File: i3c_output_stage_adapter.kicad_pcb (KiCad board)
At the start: 2 copper layers, 61 x 49.5 mm, 52 parts, among them J1 PinSocket_2x12_P2.54mm_Drill1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, J2 PinSocket_2x6_P2.54mm_Drill1.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, J3 Molex_Nano-Fit_1x2_SMD_105430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, J4 PinHeader_2x5_P1.27mm_SMD, J5 PinHeader_2x5_P1.27mm_SMD, J6 JST_XH_1x3_S3B-XH-A-LF-SN, Q1 DMC2400UV-7, Q2 DMC2400UV-7, Q3 DMC2400UV-7, Q4 DMC2400UV-7, U1 TPS7A0518P_SOT23-5, U2 SN74LVC1G240_SC70, U3 SN74LVC1G240_SC70

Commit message: [#68164] Clean DRC
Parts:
- removed D3: LED_G_0402_VLMTG1500-GS08, antmicro-footprints:LED_0402_1005Metric_G
- removed J4, J5: PinHeader_2x5_P1.27mm_SMD, antmicro-footprints:PinHeader_2x5_P1.27mm_SMD
- added J7: PinHeader_2x10_P1.27mm_SMD, antmicro-footprints:PinHeader_2x10_P1.27mm_SMD, B.Cu at (162.8, 112.0)
- added MP1: MP_Pad6mm_Drill3.2mm, antmicro-footprints:MP_Pad6mm_Drill3.2mm, F.Cu at (168.5, 76.0)
- added MP2: MP_Pad6mm_Drill3.2mm, antmicro-footprints:MP_Pad6mm_Drill3.2mm, F.Cu at (168.5, 105.0)
- added MP3: MP_Pad6mm_Drill3.2mm, antmicro-footprints:MP_Pad6mm_Drill3.2mm, F.Cu at (124.0, 86.5)
- added MP4: MP_Pad6mm_Drill3.2mm, antmicro-footprints:MP_Pad6mm_Drill3.2mm, F.Cu at (124.0, 118.5)
- added R20: R_10k_0402, antmicro-footprints:R_0402_1005Metric, F.Cu at (134.7, 99.6)
- added R21: R_0R_0402, antmicro-footprints:R_0402_1005Metric, F.Cu at (134.7, 97.6)
- added R22: R_2k_0402, antmicro-footprints:R_0402_1005Metric, F.Cu at (132.8, 111.8)
- added R23: R_2k_0402, antmicro-footprints:R_0402_1005Metric, F.Cu at (132.9, 108.4)
- added R24: R_10k_0402, antmicro-footprints:R_0402_1005Metric, F.Cu at (134.7, 111.6)
- added R25: R_0R_0402, antmicro-footprints:R_0402_1005Metric, F.Cu at (134.7, 109.6)
- Q1, Q2: value DMC2400UV-7 -> DMC31D5UDJ; footprint antmicro-footprints:SOT-563 -> antmicro-footprints:SOT-963
- R10, R19: value R_2k_0402 -> R_10k_0402
- R9: value R_2k_0402 -> R_0R_0402
- moved R19 32.1 mm to (131.1, 98.8), turned to 90 degrees
- moved R15 13.6 mm to (131.1, 96.8)
- moved TP3 6.34 mm to (163.8, 119.4)
- moved C1 5.51 mm to (141.0, 78.2), turned to -90 degrees
- moved J6 4.72 mm to (164.7, 98.0), turned to 90 degrees
- moved J1 4.66 mm to (110.0, 120.2)
- moved R16 4.05 mm to (136.0, 80.5)
- moved R10 3.84 mm to (131.1, 110.8), turned to 90 degrees
- moved R9 3.80 mm to (131.1, 108.8)
- moved J3 3.76 mm to (130.0, 76.5)
- moved R4 3.66 mm to (123.4, 110.5), turned to -90 degrees
- moved R8 3.48 mm to (125.8, 112.0), turned to 0 degrees
- moved R6 3.44 mm to (126.0, 109.1), turned to 90 degrees
- moved TP1 3.19 mm to (170.2, 119.4)
- moved TP2 3.19 mm to (167.0, 119.4)
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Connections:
- C3 pad 2: VCC -> +1V8
- C4 pad 2: VCC -> +1V8
- F1 pad 2: VCC -> +1V8
- F2 pad 2: VCC -> +1V8
- J3 pad 1: VCC -> +1V8
- J6 pad 1: /SDA -> /SCL
- J6 pad 3: /SCL -> /SDA
- Q3 pad 2: /SCL_DOWN -> Net-(Q3-G1)
- Q3 pad 4: Net-(Q3-D1) -> /SCL
- Q3 pad 5: /SCL_UP -> Net-(Q3-G2)
- Q3 pad 6: Net-(Q3-D1) -> /SCL
- Q4 pad 2: /SDA_DOWN -> Net-(Q4-G1)
- Q4 pad 5: /SDA_UP -> Net-(Q4-G2)
- R10 pad 2: Net-(Q3-S1) -> Net-(Q3-G1)
- R11 pad 2: VCC -> +1V8
- R13 pad 2: VCC -> +1V8
- R14 pad 2: VCC -> +1V8
- R15 pad 1: +3V3 -> /SDA_DOWN
- R15 pad 2: VCC -> Net-(Q4-G1)
- R16 pad 2: VCC -> +1V8
- R17 pad 2: /1V8_LDO -> +1V8
- R19 pad 1: Net-(D3-A) -> GND
- R19 pad 2: VCC -> Net-(Q4-G1)
- R5 pad 2: VCC -> +1V8
- R6 pad 2: VCC -> +1V8
- R9 pad 1: Net-(Q3-D2) -> /SCL_DOWN
- R9 pad 2: VCC -> Net-(Q3-G1)
- U2 pad 5: VCC -> +1V8
- U3 pad 5: VCC -> +1V8
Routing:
- net /SCL: track 0.00 -> 121.7 mm, vias 0 -> 5
- net /SDA: track 0.00 -> 110.2 mm, vias 0 -> 4
- net /SDA_EN/PULL: track 0.00 -> 94.4 mm, vias 0 -> 3
- net /SDA_IN/PUSH: track 0.00 -> 88.3 mm, vias 0 -> 4
- net /SDA_DOWN: track 0.00 -> 84.4 mm, vias 0 -> 3
- net /SCL_DOWN: track 0.00 -> 83.9 mm, vias 0 -> 2
- net /SDA_UP: track 0.00 -> 81.1 mm, vias 0 -> 3
- net /SCL_EN/PULL: track 0.00 -> 80.2 mm, vias 0 -> 2
- net /SCL_UP: track 0.00 -> 79.2 mm, vias 0 -> 2
- net /SCL_IN/PUSH: track 0.00 -> 77.4 mm, vias 0 -> 2
- net GND: track 0.00 -> 43.4 mm, vias 0 -> 31
- net +3V3: track 0.00 -> 32.6 mm
- net +1V8: track 0.00 -> 22.2 mm, vias 0 -> 17
- net /1V8_LDO: track 0.00 -> 4.21 mm
- net Net-(Q2-G2): track 0.00 -> 3.98 mm
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- added copper zone on In1.Cu, net +1V8
- added copper zone on In2.Cu, net GND
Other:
- board size 61 x 49.5 mm -> 72.5 x 50 mm
- copper layers 2 -> 4
- board text added: "1V8 IN"
- board text added: "I3C OUTPUT"
- board text added: "LOGIC ANALYZER CONNECTOR"
- board text added: "PMOD"
- board text removed: "VCC"

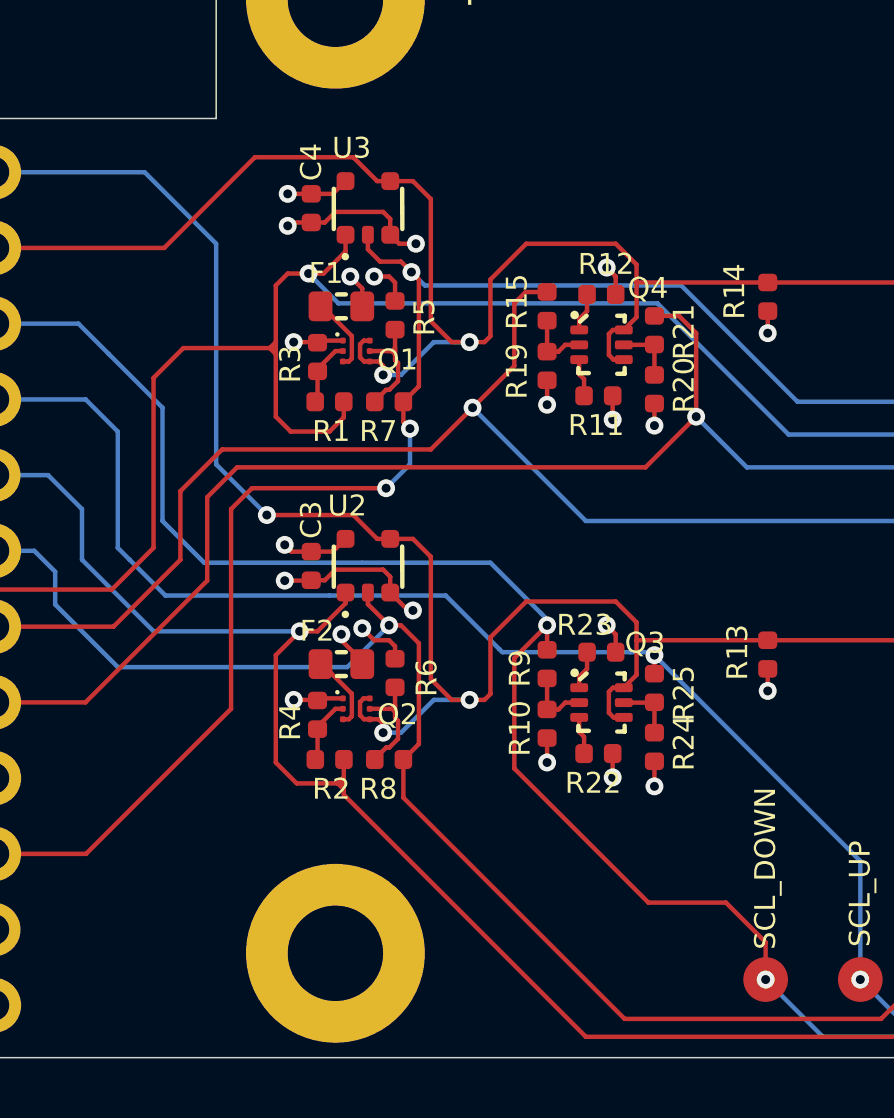
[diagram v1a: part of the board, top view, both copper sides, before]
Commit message: [#68164] Update PMOS connections on PCB
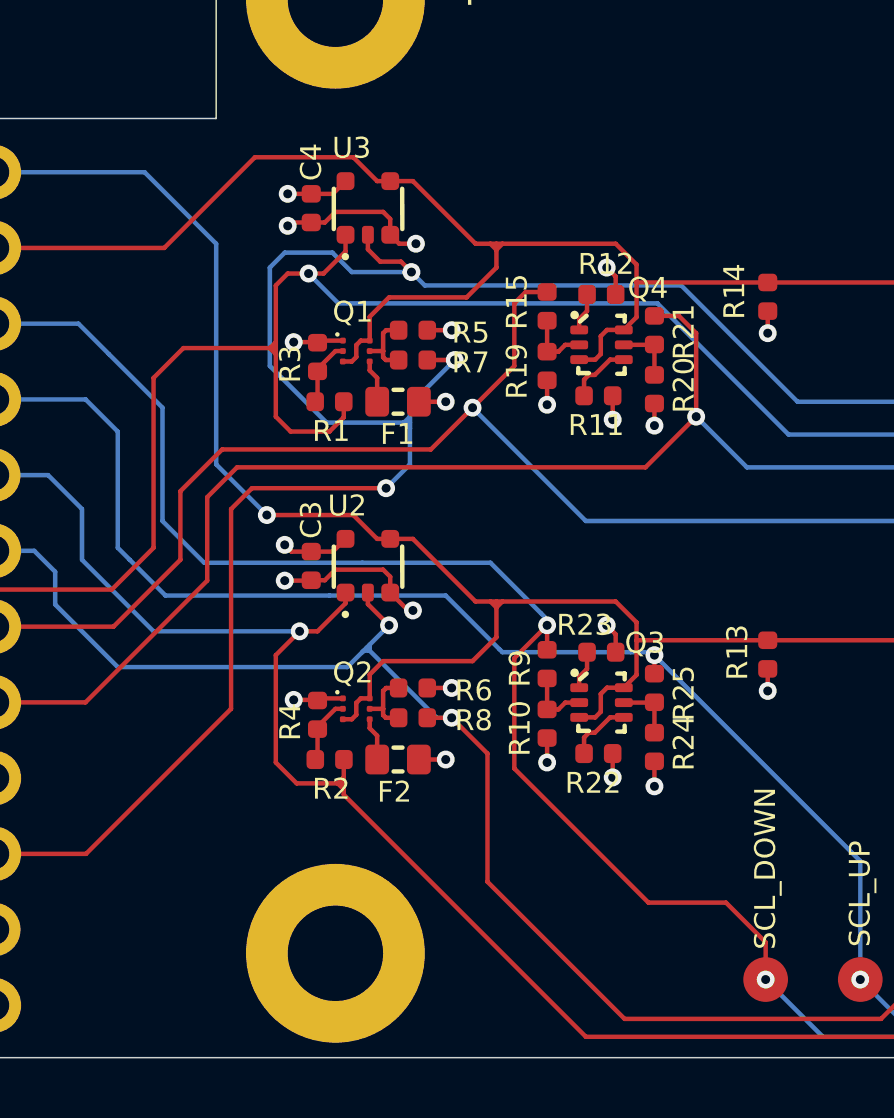
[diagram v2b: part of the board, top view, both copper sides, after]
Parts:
- moved F1 3.72 mm to (126.1, 100.0)
- moved F2 3.72 mm to (126.1, 112.0)
- moved R7 1.61 mm to (126.6, 98.6)
- moved R8 1.61 mm to (126.6, 110.6)
- moved R5 0.78 mm to (126.6, 97.6), turned to 0 degrees
- moved R6 0.78 mm to (126.6, 109.6), turned to 0 degrees
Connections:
- F1 pad 1: Net-(Q1-D2) -> Net-(Q1-S2)
- F2 pad 1: Net-(Q2-D2) -> Net-(Q2-S2)
- Q1 pad 3: Net-(Q1-D2) -> /SDA
- Q1 pad 4: /SDA -> Net-(Q1-S2)
- Q2 pad 3: Net-(Q2-D2) -> /SCL
- Q2 pad 4: /SCL -> Net-(Q2-S2)
- Q3 pad 3: Net-(Q3-D2) -> /SCL
- Q3 pad 4: /SCL -> Net-(Q3-S2)
- Q4 pad 3: Net-(Q4-D2) -> /SDA
- Q4 pad 4: /SDA -> Net-(Q4-S2)
- R11 pad 1: Net-(Q4-D2) -> Net-(Q4-S2)
- R22 pad 1: Net-(Q3-D2) -> Net-(Q3-S2)
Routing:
- net /SDA_IN/PUSH: track 88.3 -> 101.1 mm
- net /SDA: track 110.2 -> 107.5 mm, vias 4 -> 2
- net Net-(Q2-D2): track 2.56 -> 0.00 mm
- net Net-(Q1-D2): track 2.56 -> 0.00 mm
- net /SCL: track 121.7 -> 119.3 mm, vias 5 -> 3
- net +1V8: track 22.2 -> 20.0 mm
- net Net-(Q4-S2): track 0.00 -> 2.15 mm
- net Net-(Q3-S2): track 0.00 -> 2.15 mm
- net Net-(Q2-G2): track 3.98 -> 2.38 mm
- net Net-(Q1-G2): track 3.98 -> 2.38 mm
- net Net-(Q2-S2): track 0.00 -> 1.45 mm
- net Net-(Q1-S2): track 0.00 -> 1.45 mm
- net Net-(Q4-D2): track 1.28 -> 0.00 mm
- net Net-(Q3-D2): track 1.28 -> 0.00 mm
- net /SCL_IN/PUSH: track 77.4 -> 77.9 mm, vias 2 -> 3

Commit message: [#68164] Add logos, align mounting holes
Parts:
- added REF**: LOGO, antmicro-footprints:oshw-logo, F.Cu at (156.4, 105.1)
- added REF**: LOGO, antmicro-footprints:antmicro-logo_scaled_12mm, F.Cu at (138.6, 89.8)
- moved MP2 13.5 mm to (168.5, 118.5)
- moved MP3 10.5 mm to (124.0, 76.0)
- moved TP1 7.77 mm to (162.4, 119.4)
- moved TP11 7.77 mm to (130.7, 119.4)
- moved TP3 7.77 mm to (156.1, 119.4)
- moved TP4 7.77 mm to (152.9, 119.4)
- moved TP5 7.77 mm to (149.7, 119.4)
- moved TP7 7.77 mm to (143.3, 119.4)
- moved TP8 7.77 mm to (140.2, 119.4)
- moved TP9 7.77 mm to (137.0, 119.4)
- moved TP10 7.77 mm to (133.8, 119.4)
- moved TP2 7.77 mm to (159.2, 119.4)
- moved TP6 7.77 mm to (146.5, 119.4)
- moved J7 2.84 mm to (162.8, 109.1)
- moved C1 2.49 mm to (143.5, 78.2)
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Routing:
- net /SDA: track 107.5 -> 101.4 mm
- net /SCL: track 119.3 -> 124.6 mm
- net /SCL_UP: track 79.2 -> 83.9 mm
- net /SDA_EN/PULL: track 94.4 -> 97.5 mm
- net +3V3: track 32.6 -> 30.1 mm
- net /SCL_DOWN: track 83.9 -> 85.9 mm
- net /SDA_UP: track 81.1 -> 82.2 mm
- net /SDA_IN/PUSH: track 101.1 -> 100.2 mm
- net /SCL_EN/PULL: track 80.2 -> 81.0 mm
- net /SDA_DOWN: track 84.4 -> 85.0 mm
- net /SCL_IN/PUSH: track 77.9 -> 78.5 mm
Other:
- board text added: "I3C Output Stage Adapter"
- board text added: "Rev. ${REVISION}"
- board text added: "SHA: ########"

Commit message: [#68164] Apply changes to PCB
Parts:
- added C5: C_10n_0402, antmicro-footprints:C_0402_1005Metric, F.Cu at (148.3, 99.6)
- added C6: C_100n_16V_X7R_0402, antmicro-footprints:C_0402_1005Metric, F.Cu at (150.1, 101.8)
- added C7: C_1u_0603, antmicro-footprints:C_0603_1608Metric, F.Cu at (135.1, 125.5)
- added C8: C_1u_0603, antmicro-footprints:C_0603_1608Metric, F.Cu at (135.0, 121.2)
- added C9: C_1u_0603, antmicro-footprints:C_0603_1608Metric, F.Cu at (135.0, 119.8)
- added D3: LED_G_0402_VLMTG1500-GS08, antmicro-footprints:LED_0402_1005Metric_G, F.Cu at (141.7, 96.4)
- added J4: USB-C_CUI_UJC-HP-3-SMT-TR, antmicro-footprints:USB-C_Receptacle_CUI_UJC-HP-3-SMT-TR, F.Cu at (148.0, 94.5)
- added J5: PinHeader_1x3_P2.54mm_Drill1.1mm, antmicro-footprints:PinHeader_1x3_P2.54mm_Drill1.1mm, F.Cu at (131.5, 120.5)
- added L1: FB_120Z_2A_Murata-BLM18PG_0603, antmicro-footprints:FB_0603_1608Metric, F.Cu at (151.7, 99.3)
- added L2: FB_120Z_2A_Murata-BLM18PG_0603, antmicro-footprints:FB_0603_1608Metric, F.Cu at (149.6, 99.9)
- added Q5: DMG1012T-7, antmicro-footprints:SOT-523, F.Cu at (135.2, 96.6)
- added R26: R_5k1_0402, antmicro-footprints:R_0402_1005Metric, F.Cu at (147.2, 99.6)
- added R27: R_5k1_0402, antmicro-footprints:R_0402_1005Metric, F.Cu at (146.0, 99.6)
- added R28: 4x0R_0402_array, antmicro-footprints:4x0R_0402_array_EXB28V, F.Cu at (105.2, 109.0)
- added R29: R_2k_0402, antmicro-footprints:R_0402_1005Metric, F.Cu at (141.7, 98.6)
- added R30: R_10k_0402, antmicro-footprints:R_0402_1005Metric, F.Cu at (135.2, 98.5)
- added REF**: Jumper_1x2_P2.54mm, antmicro-footprints:Jumper_1x2_P2.54mm, F.Cu at (129.0, 120.5)
- added U4: TLV70033_SC70, antmicro-footprints:SC-70-5, F.Cu at (135.1, 123.4)
- J1, J2: moved to B.Cu
- J3: value Molex_Nano-Fit_1x2_SMD_1054301202 -> JST_SH_1x4_SM04B-SRSS-TB-LF-SN; footprint antmicro-footprints:Conn_Molex_Nano-Fit_1x2_SMD_1054301202 -> antmicro-footprints:Conn_JST_SH_1x4_SM04B-SRSS-TB-LF-SN
- J6: value JST_XH_1x3_S3B-XH-A-LF-SN -> PinHeader_1x3_P2.54mm_Drill1.1mm_Horizontal; footprint antmicro-footprints:Conn_JST_XH_1x3_S3B-XH-A-LF-SN -> antmicro-footprints:PinHeader_1x3_P2.54mm_Horizontal
- J7: moved to F.Cu
- moved C1 48.7 mm to (127.7, 124.2), turned to 90 degrees
- moved J3 48.4 mm to (172.0, 104.5), turned to 90 degrees
- moved J2 47.4 mm to (110.0, 112.6), turned to -90 degrees
- moved U1 47.3 mm to (130.1, 124.2), turned to -90 degrees
- moved C2 47.2 mm to (132.6, 125.2), turned to 90 degrees
- moved R16 43.1 mm to (132.6, 123.2), turned to 90 degrees
- moved TP11 35.6 mm to (165.7, 125.7)
- moved D1 30.4 mm to (137.7, 96.4), turned to -90 degrees
- moved TP10 30.0 mm to (163.2, 125.7)
- moved R17 29.5 mm to (137.7, 98.6), turned to -90 degrees
- moved J1 27.9 mm to (110.0, 92.3), turned to -90 degrees
- moved D2 27.8 mm to (139.7, 96.4), turned to -90 degrees
- moved R18 26.8 mm to (139.7, 98.6), turned to -90 degrees
- moved TP9 24.5 mm to (160.7, 125.7)
- moved TP1 23.0 mm to (140.3, 125.7)
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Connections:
- D1 pad 1: GND -> Net-(D1-C)
- J1 pad 10: /SDA_UP -> /SDA_IN/PUSH
- J1 pad 12: /SDA_DOWN -> /SDA_EN/PULL
- J1 pad 14: /SCL_IN/PUSH -> /SDA_UP
- J1 pad 16: /SCL_EN/PULL -> /SCL_DOWN
- J1 pad 17: GND -> /PMOD1
- J1 pad 18: /SCL_UP -> /SCL
- J1 pad 19: GND -> /PMOD3
- J1 pad 20: /SCL_DOWN -> /SCL_IN/PUSH
- J1 pad 21: GND -> /PMOD5
- J1 pad 22: /SDA -> /SCL_EN/PULL
- J1 pad 23: GND -> /PMOD7
- J1 pad 24: /SCL -> /SCL_UP
- J1 pad 6: /SDA_IN/PUSH -> /SDA_DOWN
- J1 pad 8: /SDA_EN/PULL -> /SDA
- J2 pad 1: unconnected-(J2-Pad1) -> /PMOD1
- J2 pad 11: +3V3 -> /PMOD_3V3
- J2 pad 12: +3V3 -> /PMOD_3V3
- J2 pad 2: unconnected-(J2-Pad2) -> /SCL
- J2 pad 3: unconnected-(J2-Pad3) -> /PMOD3
- J2 pad 4: unconnected-(J2-Pad4) -> /SCL_IN/PUSH
- J2 pad 5: unconnected-(J2-Pad5) -> /PMOD5
- J2 pad 6: unconnected-(J2-Pad6) -> /SCL_EN/PULL
- J2 pad 7: unconnected-(J2-Pad7) -> /PMOD7
- J2 pad 8: unconnected-(J2-Pad8) -> /SCL_UP
- J3 pad 1: +1V8 -> GND
- J3 pad 2: GND -> +3V3
- R17 pad 2: +1V8 -> +3V3
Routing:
- net +5V: track 0.00 -> 49.5 mm, vias 0 -> 4
- net /SDA: track 101.4 -> 147.5 mm
- net +3V3: track 30.1 -> 69.7 mm, vias 0 -> 3
- net /PMOD_3V3: track 0.00 -> 20.9 mm
- net GNDREF: track 0.00 -> 18.3 mm
- net /PMOD7: track 0.00 -> 15.1 mm
- net /PMOD5: track 0.00 -> 12.6 mm
- net /SDA_UP: track 82.2 -> 94.6 mm
- net GND: track 43.4 -> 54.8 mm, vias 31 -> 39
- net /PMOD3: track 0.00 -> 9.58 mm
- net Net-(C5-Pad1): track 0.00 -> 8.06 mm
- net /SDA_IN/PUSH: track 100.2 -> 106.7 mm, vias 4 -> 3
- net /SCL_DOWN: track 85.9 -> 79.6 mm
- net /SCL_IN/PUSH: track 78.5 -> 84.6 mm, vias 3 -> 2
- net /PMOD1: track 0.00 -> 5.92 mm
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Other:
- board size 72.5 x 50 mm -> 75 x 36.5 mm
- board text added: "+5V"
- board text added: "QWIIC"
- board text added: "SCL_EN"
- board text added: "SCL_IN"
- board text added: "SDA_EN"
- board text added: "SDA_IN"
- board text removed: "1V8 IN"
- board text removed: "PMOD"
- board text removed: "SCL_EN/PULL"
- board text removed: "SCL_IN/PUSH"
- board text removed: "SDA_EN/PULL"
- board text removed: "SDA_IN/PUSH"

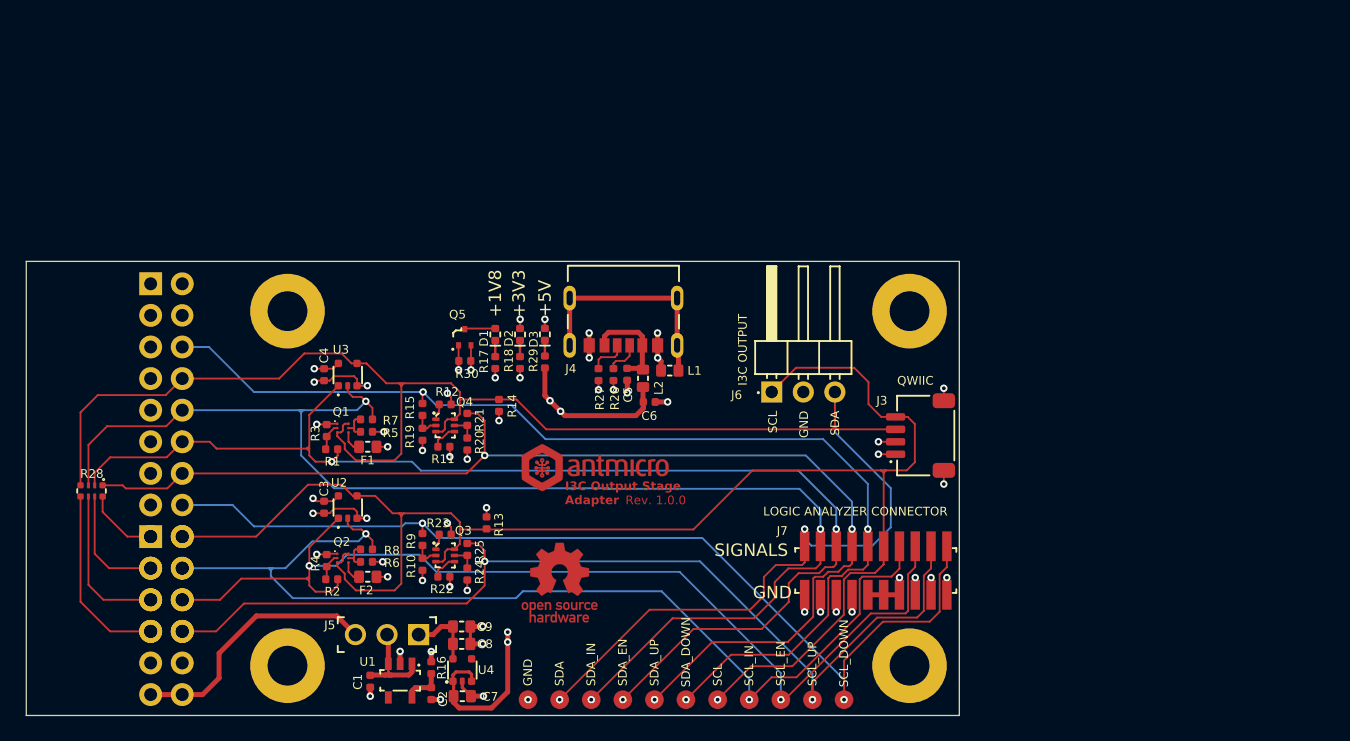
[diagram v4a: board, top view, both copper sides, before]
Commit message: [#68164] Update components, rotate PCB
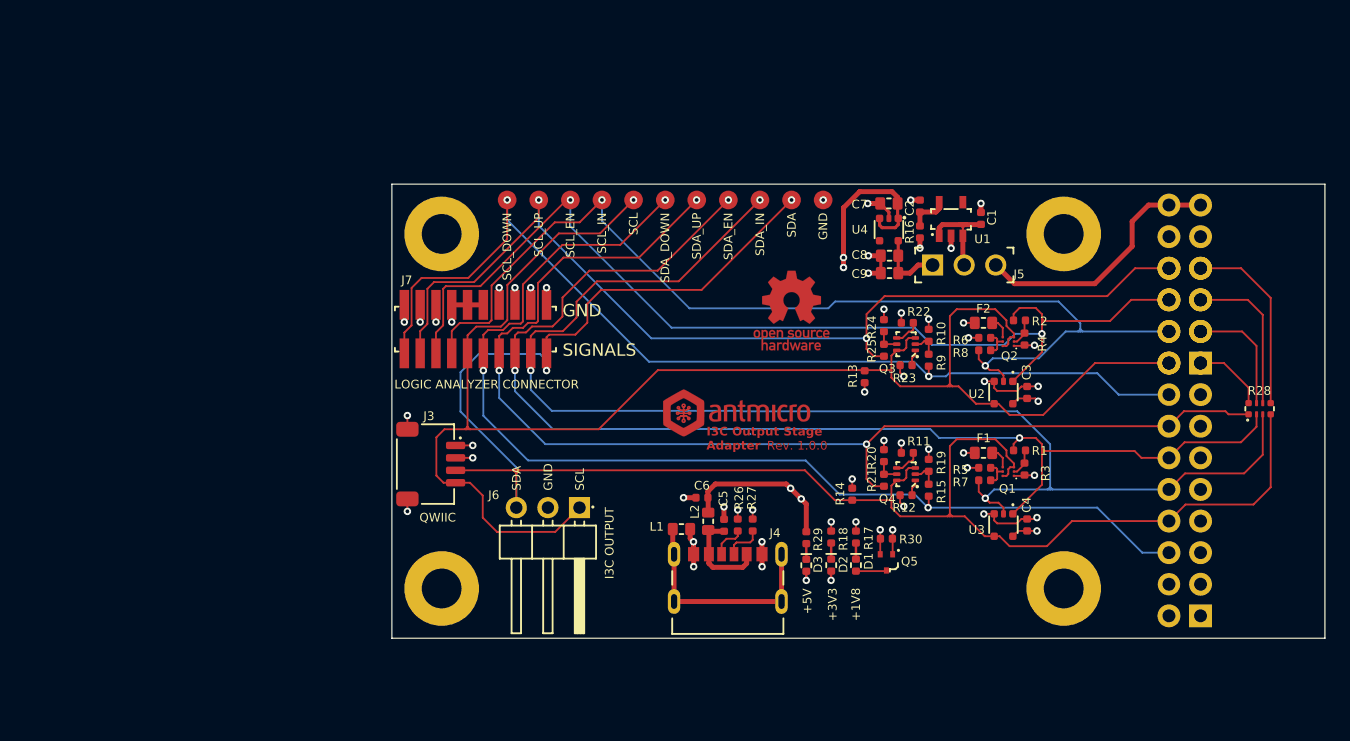
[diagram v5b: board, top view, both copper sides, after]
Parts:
- moved R28 94.1 mm to (199.1, 102.3), turned to 0 degrees
- moved J1 88.5 mm to (194.4, 119.0), turned to 90 degrees
- moved J2 85.5 mm to (194.4, 98.7), turned to 90 degrees
- moved MP4 71.4 mm to (183.4, 88.3), turned to 180 degrees
- moved MP3 66.3 mm to (183.4, 116.8), turned to 180 degrees
- moved C1 61.6 mm to (176.7, 87.0), turned to -90 degrees
- moved R2 59.1 mm to (179.8, 95.2), turned to 0 degrees
- moved R4 58.9 mm to (180.2, 96.7), turned to 90 degrees
- moved C4 57.8 mm to (180.5, 111.7), turned to -90 degrees
- moved U1 57.8 mm to (174.3, 87.1), turned to 90 degrees
- moved C3 57.3 mm to (180.5, 101.0), turned to -90 degrees
- moved Q2 56.3 mm to (178.9, 96.9), turned to 180 degrees
- moved R3 56.2 mm to (180.2, 107.2), turned to 90 degrees
- moved C2 55.5 mm to (171.8, 86.1), turned to -90 degrees
- moved R1 55.3 mm to (179.8, 105.7), turned to 0 degrees
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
